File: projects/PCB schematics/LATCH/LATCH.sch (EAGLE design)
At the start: 18 parts, among them Q2 IRLZ44Z

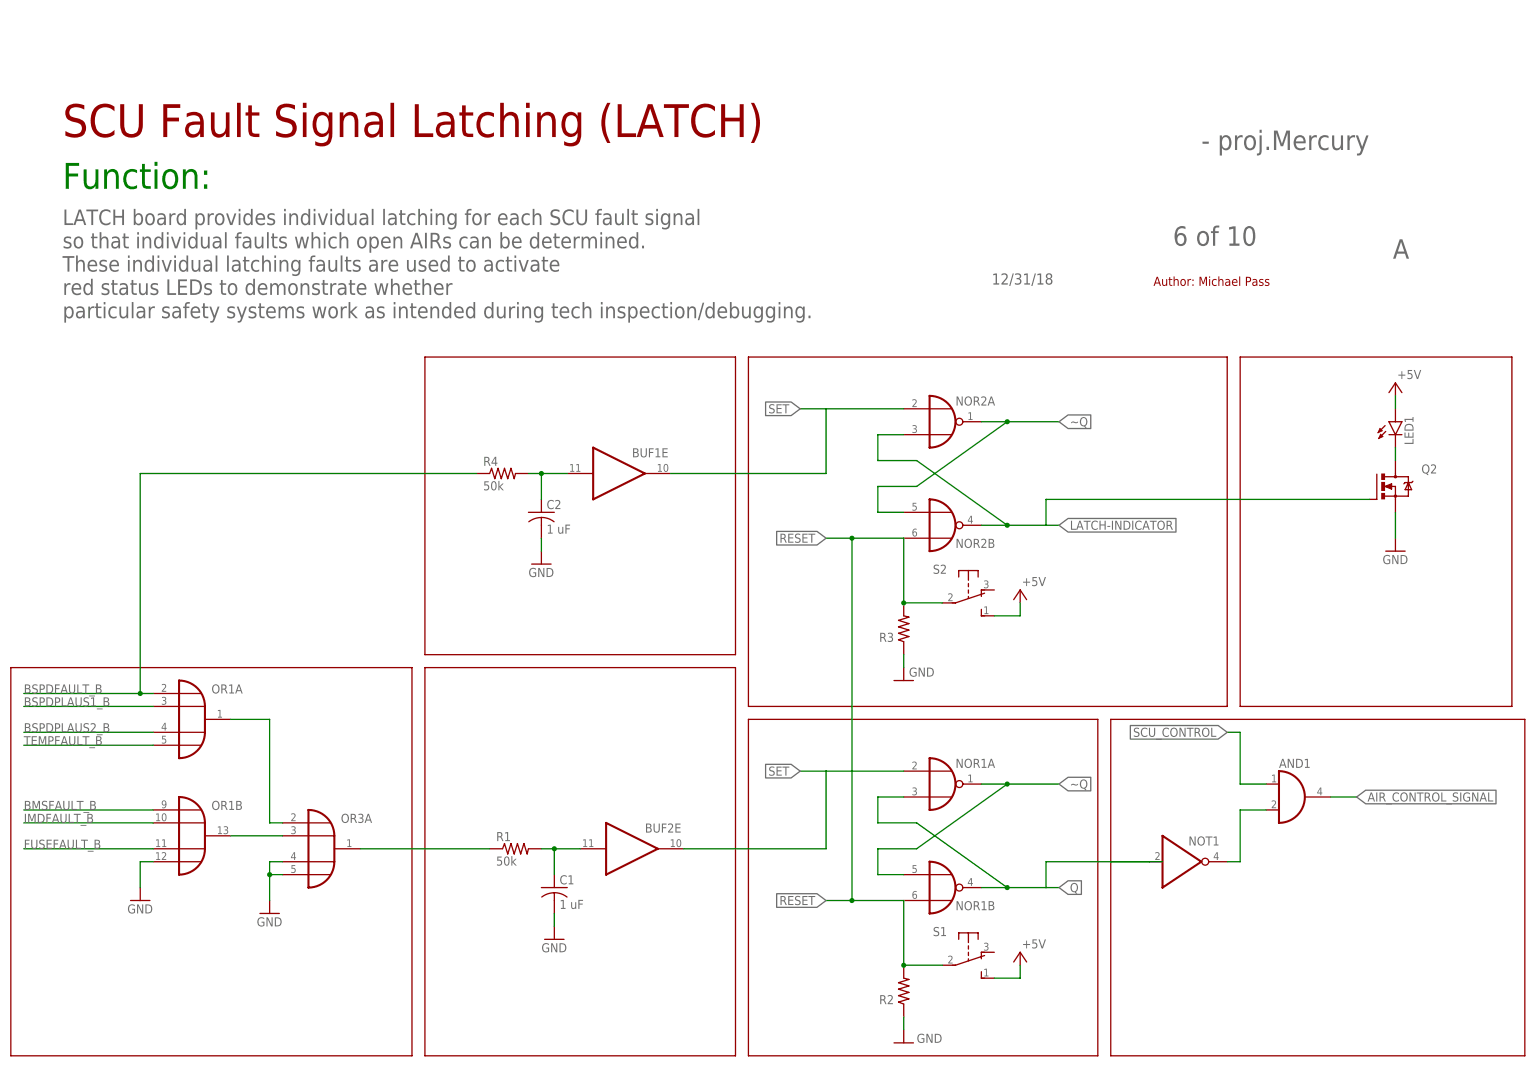
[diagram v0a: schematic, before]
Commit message: SC - Rev A; First PCB revision complete.
This marks the first draft of the SC board.
Parts have been laid out and initial routing completed through
extensive use of autorouter.
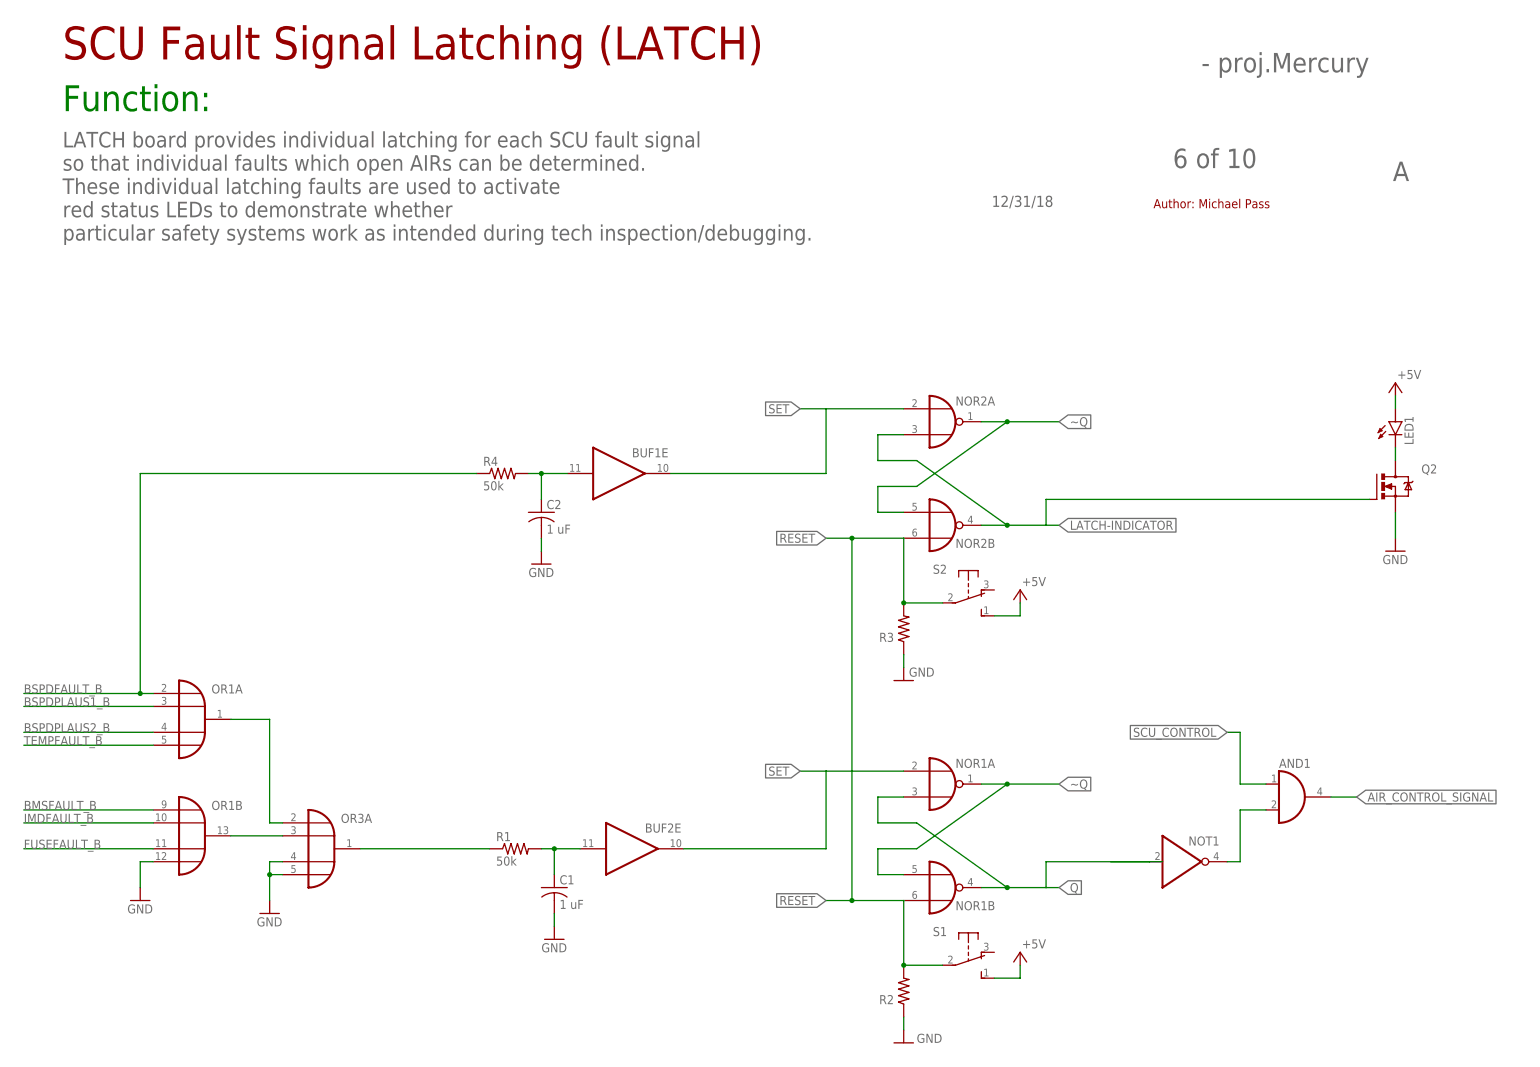
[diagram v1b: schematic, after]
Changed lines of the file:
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@@
 <?xml version="1.0" encoding="utf-8"?>
 <!DOCTYPE eagle SYSTEM "eagle.dtd">
-<eagle version="9.3.0">
+<eagle version="9.3.1">
 <drawing>
 <settings>
@@
 <sheet>
 <plain>
-<text x="195.58" y="182.88" size="5.08" layer="100">Iowa</text>
-<text x="210.82" y="182.88" size="5.08" layer="98">Formula</text>
-<text x="197.612" y="156.464" size="2.1844" layer="96">12/31/18</text>
-<text x="233.172" y="164.084" size="3.81" layer="96">6 of 10</text>
-<text x="238.76" y="182.88" size="3.81" layer="96">- proj.Mercury</text>
-<text x="15.24" y="185.42" size="6.4516" layer="94">SCU Fault Signal Latching (LATCH)</text>
-<text x="15.24" y="175.26" size="5.08" layer="91">Function:</text>
-<text x="15.24" y="149.86" size="3.048" layer="96">LATCH board provides individual latching for each SCU fault signal
+<text x="195.58" y="198.12" size="5.08" layer="100">Iowa</text>
+<text x="210.82" y="198.12" size="5.08" layer="98">Formula</text>
+<text x="197.612" y="171.704" size="2.1844" layer="96">12/31/18</text>
+<text x="233.172" y="179.324" size="3.81" layer="96">6 of 10</text>
+<text x="238.76" y="198.12" size="3.81" layer="96">- proj.Mercury</text>
+<text x="15.24" y="200.66" size="6.4516" layer="94">SCU Fault Signal Latching (LATCH)</text>
+<text x="15.24" y="190.5" size="5.08" layer="91">Function:</text>
+<text x="15.24" y="165.1" size="3.048" layer="96">LATCH board provides individual latching for each SCU fault signal
 so that individual faults which open AIRs can be determined.
 These individual latching faults are used to activate
 red status LEDs to demonstrate whether
 particular safety systems work as intended during tech inspection/debugging.</text>
-<text x="229.362" y="156.21" size="1.778" layer="94">Author: Michael Pass</text>
-<text x="276.352" y="161.544" size="3.81" layer="96">A</text>
-<frame x1="0" y1="0" x2="307.34" y2="205.74" columns="8" rows="5" layer="91"/>
-<wire x1="5.08" y1="5.08" x2="5.08" y2="81.28" width="0.254" layer="94"/>
-<wire x1="5.08" y1="81.28" x2="83.82" y2="81.28" width="0.254" layer="94"/>
-<wire x1="83.82" y1="81.28" x2="83.82" y2="5.08" width="0.254" layer="94"/>
-<wire x1="83.82" y1="5.08" x2="5.08" y2="5.08" width="0.254" layer="94"/>
-<wire x1="86.36" y1="5.08" x2="86.36" y2="81.28" width="0.254" layer="94"/>
-<wire x1="86.36" y1="81.28" x2="147.32" y2="81.28" width="0.254" layer="94"/>
-<wire x1="147.32" y1="81.28" x2="147.32" y2="5.08" width="0.254" layer="94"/>
-<wire x1="147.32" y1="5.08" x2="86.36" y2="5.08" width="0.254" layer="94"/>
-<wire x1="149.86" y1="5.08" x2="149.86" y2="71.12" width="0.254" layer="94"/>
-<wire x1="149.86" y1="71.12" x2="218.44" y2="71.12" width="0.254" layer="94"/>
-<wire x1="218.44" y1="71.12" x2="218.44" y2="5.08" width="0.254" layer="94"/>
-<wire x1="218.44" y1="5.08" x2="149.86" y2="5.08" width="0.254" layer="94"/>
-<wire x1="220.98" y1="5.08" x2="220.98" y2="71.12" width="0.254" layer="94"/>
-<wire x1="220.98" y1="71.12" x2="302.26" y2="71.12" width="0.254" layer="94"/>
-<wire x1="302.26" y1="71.12" x2="302.26" y2="5.08" width="0.254" layer="94"/>
-<wire x1="302.26" y1="5.08" x2="220.98" y2="5.08" width="0.254" layer="94"/>
-<wire x1="149.86" y1="73.66" x2="149.86" y2="142.24" width="0.254" layer="94"/>
-<wire x1="149.86" y1="142.24" x2="243.84" y2="142.24" width="0.254" layer="94"/>
-<wire x1="243.84" y1="142.24" x2="243.84" y2="73.66" width="0.254" layer="94"/>
-<wire x1="243.84" y1="73.66" x2="149.86" y2="73.66" width="0.254" layer="94"/>
-<wire x1="246.38" y1="142.24" x2="246.38" y2="73.66" width="0.254" layer="94"/>
-<wire x1="246.38" y1="73.66" x2="299.72" y2="73.66" width="0.254" layer="94"/>
-<wire x1="299.72" y1="73.66" x2="299.72" y2="142.24" width="0.254" layer="94"/>
-<wire x1="299.72" y1="142.24" x2="246.38" y2="142.24" width="0.254" layer="94"/>
-<wire x1="86.36" y1="83.82" x2="86.36" y2="142.24" width="0.254" layer="94"/>
-<wire x1="86.36" y1="142.24" x2="147.32" y2="142.24" width="0.254" layer="94"/>
-<wire x1="147.32" y1="142.24" x2="147.32" y2="83.82" width="0.254" layer="94"/>
-<wire x1="147.32" y1="83.82" x2="86.36" y2="83.82" width="0.254" layer="94"/>
+<text x="229.362" y="171.45" size="1.778" layer="94">Author: Michael Pass</text>
+<text x="276.352" y="176.784" size="3.81" layer="96">A</text>
 </plain>
 <instances>
@@
 <attribute name="NAME" x="236.22" y="46.355" size="1.778" layer="95"/>
 </instance>
-<instance part="FRAME2" gate="G$2" x="182.88" y="154.94" smashed="yes">
-<attribute name="SHEET" x="269.24" y="156.21" size="2.54" layer="94"/>
-<attribute name="DRAWING_NAME" x="200.66" y="173.99" size="2.54" layer="94"/>
+<instance part="FRAME2" gate="G$2" x="182.88" y="170.18" smashed="yes">
+<attribute name="SHEET" x="269.24" y="171.45" size="2.54" layer="94"/>
+<attribute name="DRAWING_NAME" x="200.66" y="189.23" size="2.54" layer="94"/>
 </instance>
 </instances>
